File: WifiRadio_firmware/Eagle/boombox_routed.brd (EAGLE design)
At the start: 64.4 x 52.1 mm, 20 parts, among them J1 POWER_JACKPTH, Y1 16 MHz

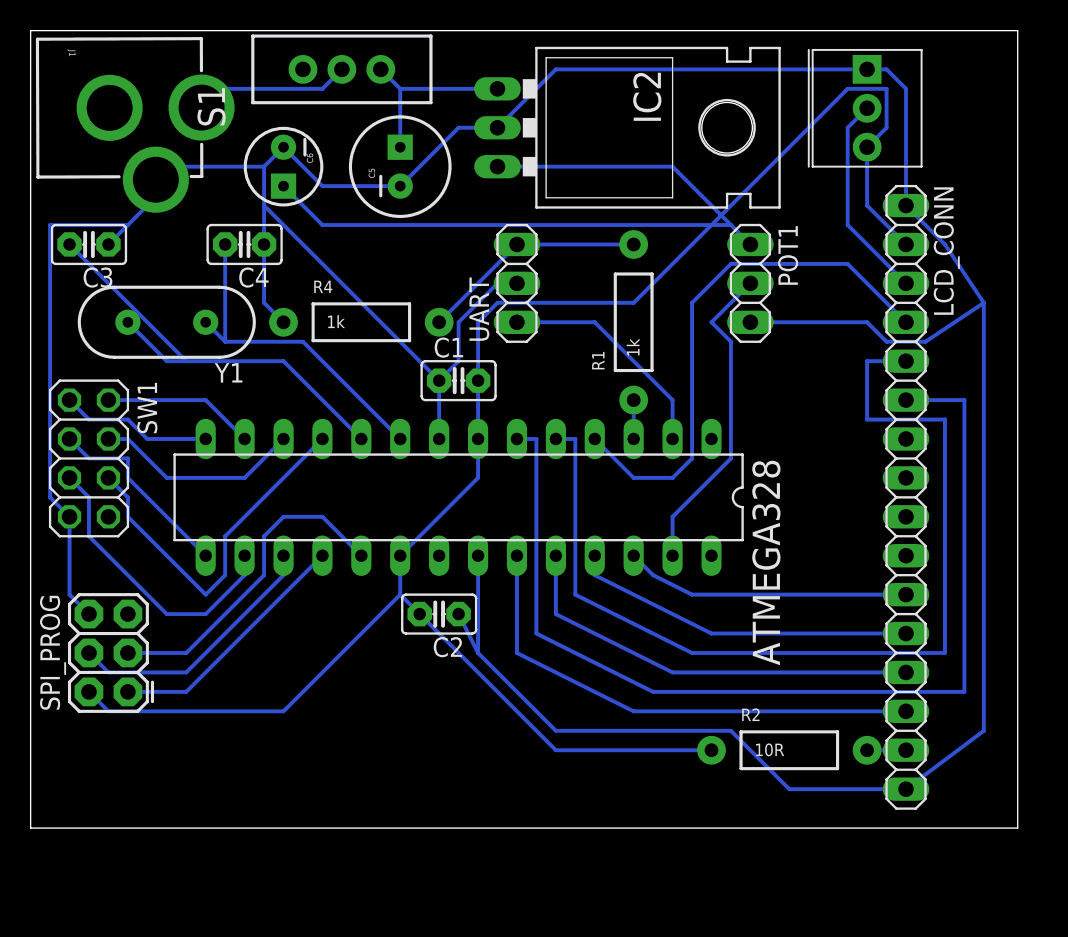
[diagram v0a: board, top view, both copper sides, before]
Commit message: Fixed DRC warnings
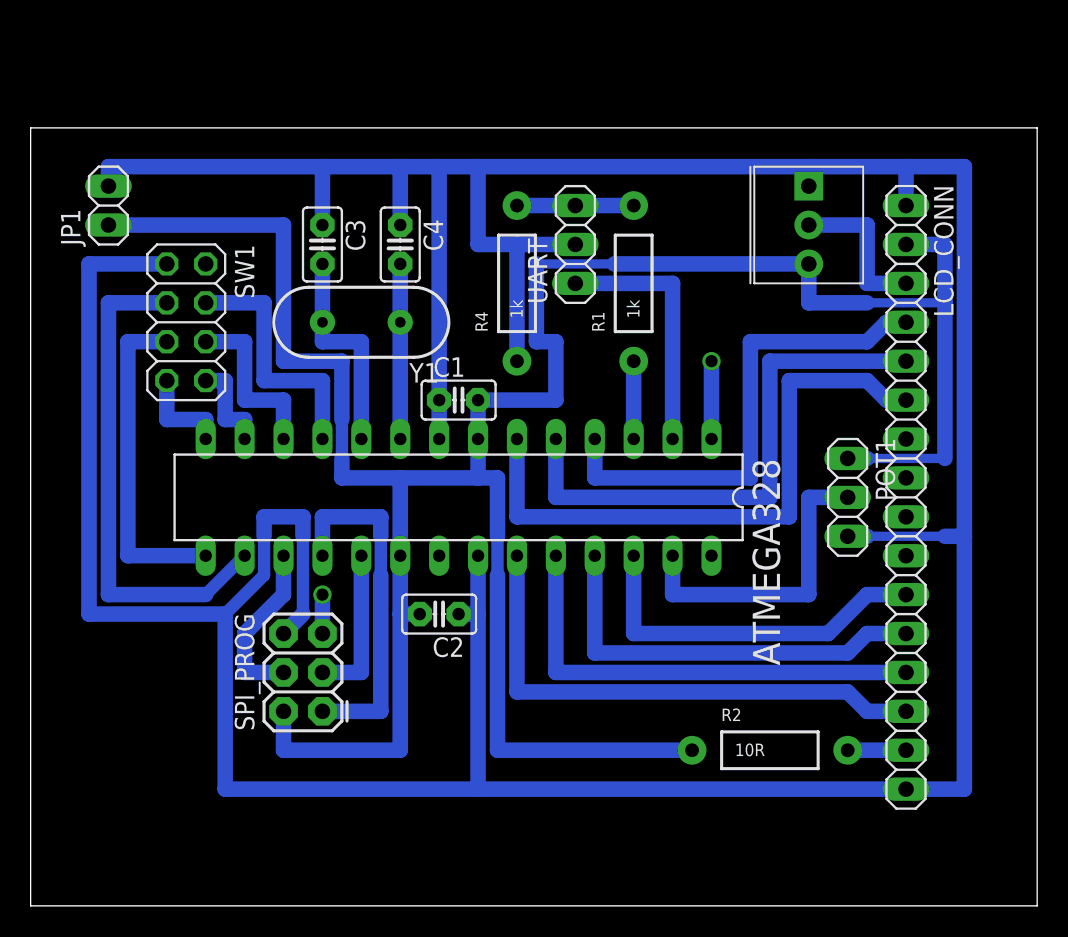
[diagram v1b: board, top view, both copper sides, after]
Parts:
- removed C5: 100uF, SparkFun:CPOL-RADIAL-100UF-25V
- removed C6: 10uF, SparkFun:CPOL-RADIAL-10UF-25V
- removed IC2: (no value), SparkFun:TO-220-ALT
- removed J1: POWER_JACKPTH, SparkFun:POWER_JACK_PTH
- removed S1: (no value), SparkFun:SWITCH-SPDT
- added JP1: (no value), pinhead:1X02
- POT1: value (none) -> 1k
- moved POT1 15.3 mm to (53.3, 22.9)
- moved C3 15.2 mm to (19.1, 39.4), turned to 270 degrees
- moved SPI_PROG 12.8 mm to (19.1, 8.89)
- moved Y1 12.7 mm to (21.6, 34.3)
- moved SW1 10.9 mm to (10.2, 34.3)
- moved R4 10.5 mm to (31.8, 36.8), turned to 90 degrees
- moved C4 10.2 mm to (24.1, 39.4), turned to 270 degrees
- moved CONTR 8.52 mm to (48.3, 43.2)
- moved UART 4.58 mm to (35.6, 39.4)
- moved R1 2.54 mm to (39.4, 36.8)
- moved R2 1.27 mm to (48.3, 6.35)
- moved C1 1.27 mm to (27.9, 29.2)
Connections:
- removed net 9V: C5.1, IC2.IN, S1.3
- removed net N$26: ATMEGA328.13, SW1.2
- removed net N$27 (its old number): ATMEGA328.14, SW1.1
- removed net N$28: ATMEGA328.15, SW1.3
- removed net N$29: ATMEGA328.16, SW1.5
- removed net N$31: J1.PWR, S1.2
- new net N$19: ATMEGA328.14, SW1.7
- new net N$21: ATMEGA328.15, SW1.5
- new net N$22: ATMEGA328.12, SW1.6
- net GND: now also JP1.2, SW1.1; no longer C5.2, C6.2, IC2.GND, J1.GNDBREAK, SW1.7
- net N$23: now also ATMEGA328.13
- net N$24: now also SW1.4; no longer SW1.6
- net N$25: now also ATMEGA328.16, SW1.3; no longer ATMEGA328.12, SW1.4
- net VCC: now also JP1.1; no longer C6.1, IC2.OUT
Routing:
- net GND: track 239.7 -> 284.8 mm
- net N$8: track 63.1 -> 35.6 mm
- net N$9: track 65.7 -> 39.9 mm
- net N$21: track 0.00 -> 21.6 mm
- net N$25: track 13.5 -> 32.8 mm
- net N$29: track 18.9 -> 0.00 mm
- net N$1: track 29.2 -> 14.0 mm
- net N$28: track 12.8 -> 0.00 mm
- net VCC: track 162.0 -> 174.0 mm
- net 9V: track 12.0 -> 0.00 mm
- net N$22: track 0.00 -> 11.4 mm
- net N$16: track 21.5 -> 10.2 mm
- net N$2: track 22.2 -> 11.4 mm
- net N$31: track 10.7 -> 0.00 mm
- net N$26: track 9.94 -> 0.00 mm
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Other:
- board size 64.4 x 52.1 mm -> 65.7 x 50.8 mm

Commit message: Finished manual routing
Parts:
- removed JP1: (no value), pinhead:1X02
- added PWR: (no value), pinhead:1X02
- moved POT1 6.35 mm to (49.5, 17.8), turned to 0 degrees
- moved R2 3.81 mm to (44.5, 6.35)
- moved CONTR 3.59 mm to (45.7, 40.6)
- moved SPI_PROG 1.27 mm to (19.1, 7.62)
- moved LCD_CONN 1.27 mm to (55.9, 22.9)
- renumbered SW1 to SW_CONN
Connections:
- net GND: now also PWR.2, SW_CONN.2; no longer JP1.2, SW_CONN.1
- net VCC: now also PWR.1; no longer JP1.1
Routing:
- net GND: track 284.8 -> 254.3 mm
- net N$20: track 20.3 -> 14.0 mm
- net N$10: track 3.81 -> 6.35 mm
- net N$3: track 10.2 -> 8.15 mm
- net N$27: track 7.62 -> 8.89 mm
- net N$18: track 11.2 -> 12.5 mm
- net N$17: track 22.9 -> 24.1 mm
- net N$16: track 10.2 -> 11.4 mm
- net N$9: track 39.9 -> 38.6 mm
- net N$8: track 35.6 -> 34.3 mm
- net N$14: track 23.9 -> 22.6 mm
- net N$13: track 27.2 -> 25.9 mm
- net N$12: track 30.5 -> 29.2 mm
- net N$11: track 34.8 -> 33.5 mm
- net N$7: track 32.3 -> 31.0 mm
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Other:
- board size 65.7 x 50.8 mm -> 59.4 x 45.7 mm
- board text added: "(C) 2012"
- board text added: "BOUWENS"
- board text added: "JEROEN"
- board text added: "REV1.0"

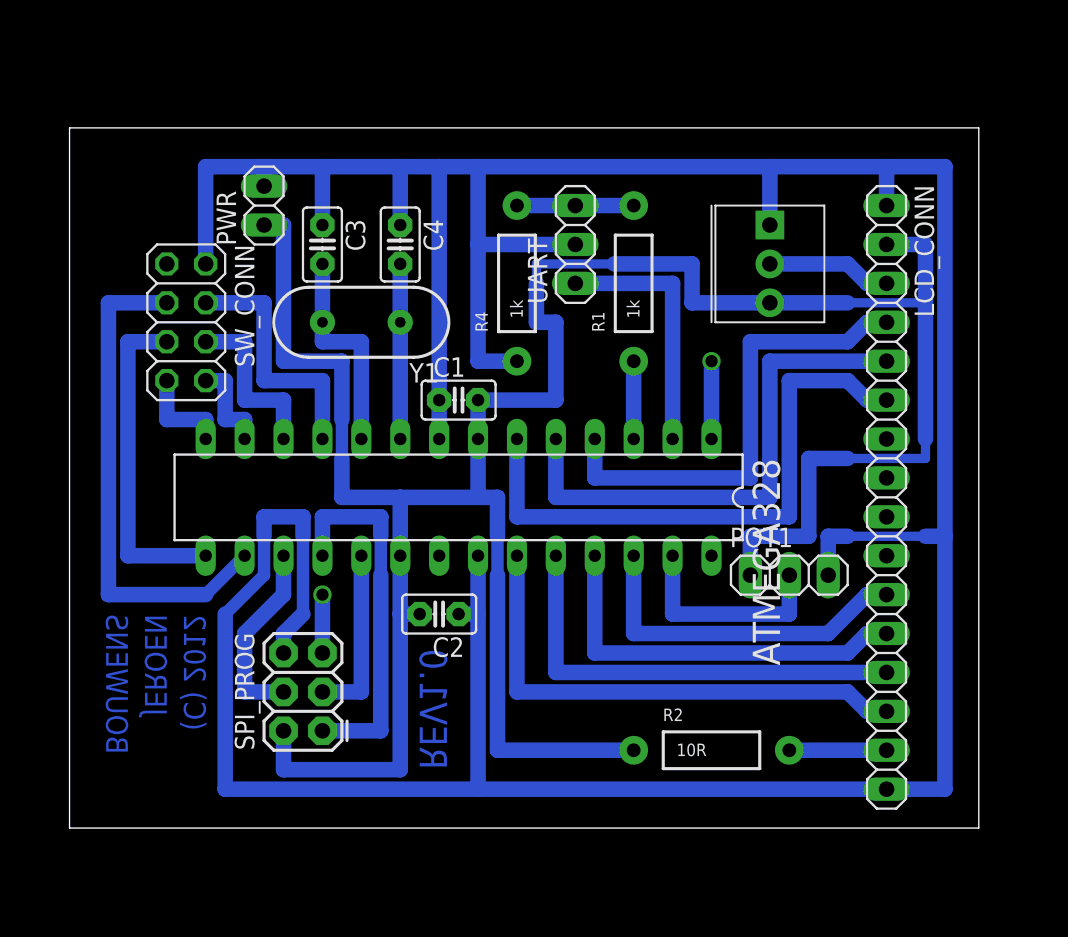
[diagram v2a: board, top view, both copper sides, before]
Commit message: Modified everything to avoid 90 degree angles
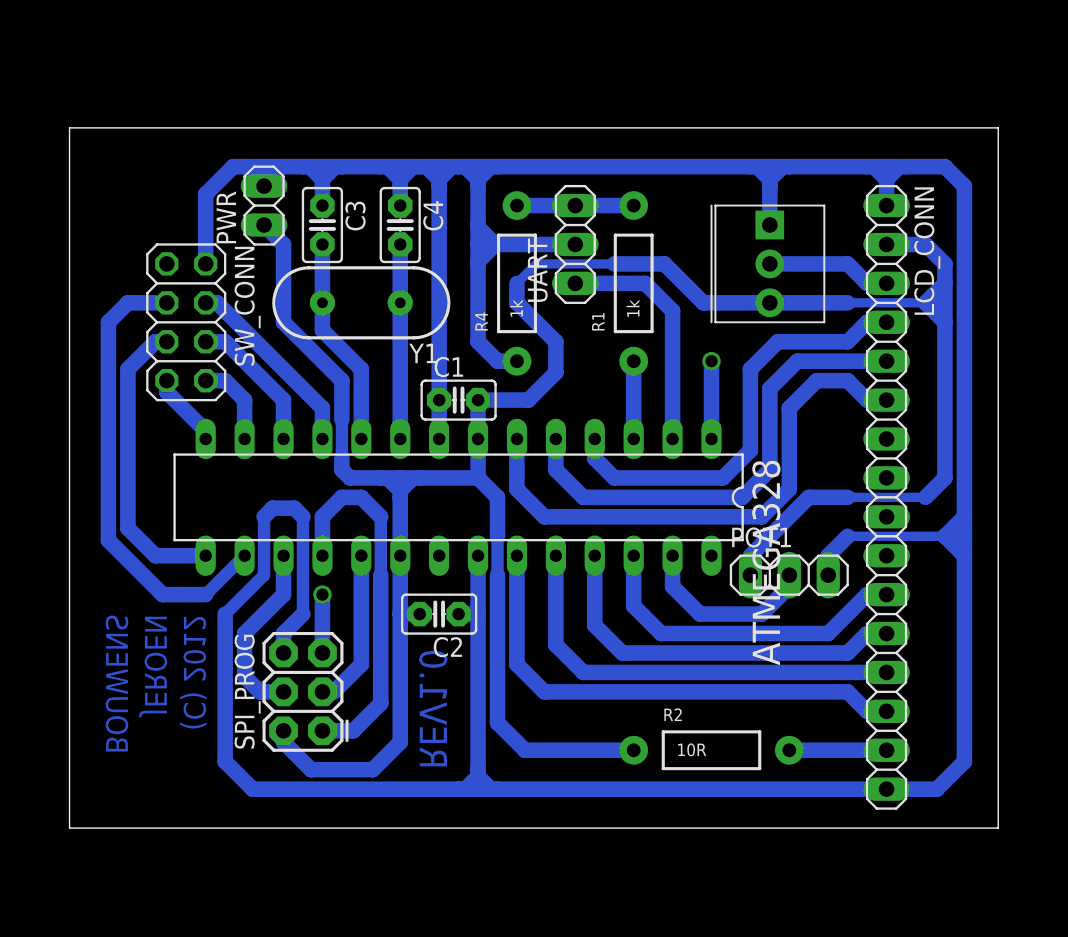
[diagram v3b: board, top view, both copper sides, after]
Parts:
- moved C3 1.27 mm to (19.1, 40.6)
- moved C4 1.27 mm to (24.1, 40.6)
- moved Y1 1.27 mm to (21.6, 35.6)
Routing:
- net GND: track 254.3 -> 310.3 mm
- net N$24: track 16.5 -> 12.5 mm
- net N$8: track 34.3 -> 31.1 mm
- net N$9: track 38.6 -> 35.5 mm
- net N$7: track 31.0 -> 28.2 mm
- net N$25: track 32.8 -> 30.0 mm
- net N$22: track 11.4 -> 9.20 mm
- net VCC: track 172.7 -> 170.6 mm
- net N$21: track 21.6 -> 19.5 mm
- net N$20: track 14.0 -> 11.9 mm
- net N$19: track 6.35 -> 4.86 mm
- net N$2: track 11.4 -> 12.7 mm
- net N$16: track 11.4 -> 10.4 mm
- net N$13: track 25.9 -> 24.9 mm
- net N$12: track 29.2 -> 28.2 mm
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- added copper zone on layer 16, net N$30
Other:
- board size 59.4 x 45.7 mm -> 60.6 x 45.7 mm

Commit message: Fixed small error
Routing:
- net VCC: track 170.6 -> 171.8 mm
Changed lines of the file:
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@@
 <wire x1="59.69" y1="34.29" x2="59.69" y2="36.83" width="1.016" layer="16"/>
 <wire x1="46.99" y1="19.05" x2="46.99" y2="17.78" width="0" layer="19" extent="16-16"/>
+<wire x1="46.99" y1="19.05" x2="46.99" y2="17.78" width="1.016" layer="16"/>
 </signal>
 <signal name="GND">
